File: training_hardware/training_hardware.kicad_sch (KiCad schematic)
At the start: 0 parts

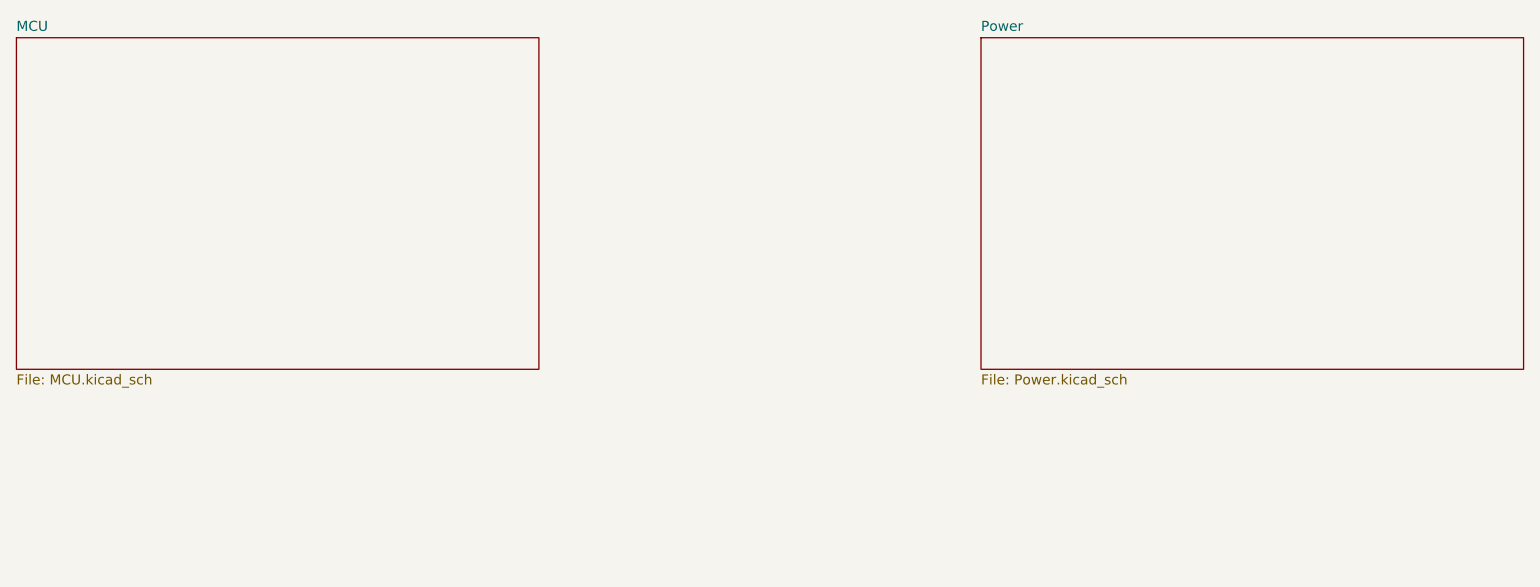
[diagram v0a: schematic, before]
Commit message: Add CAN Transceiver
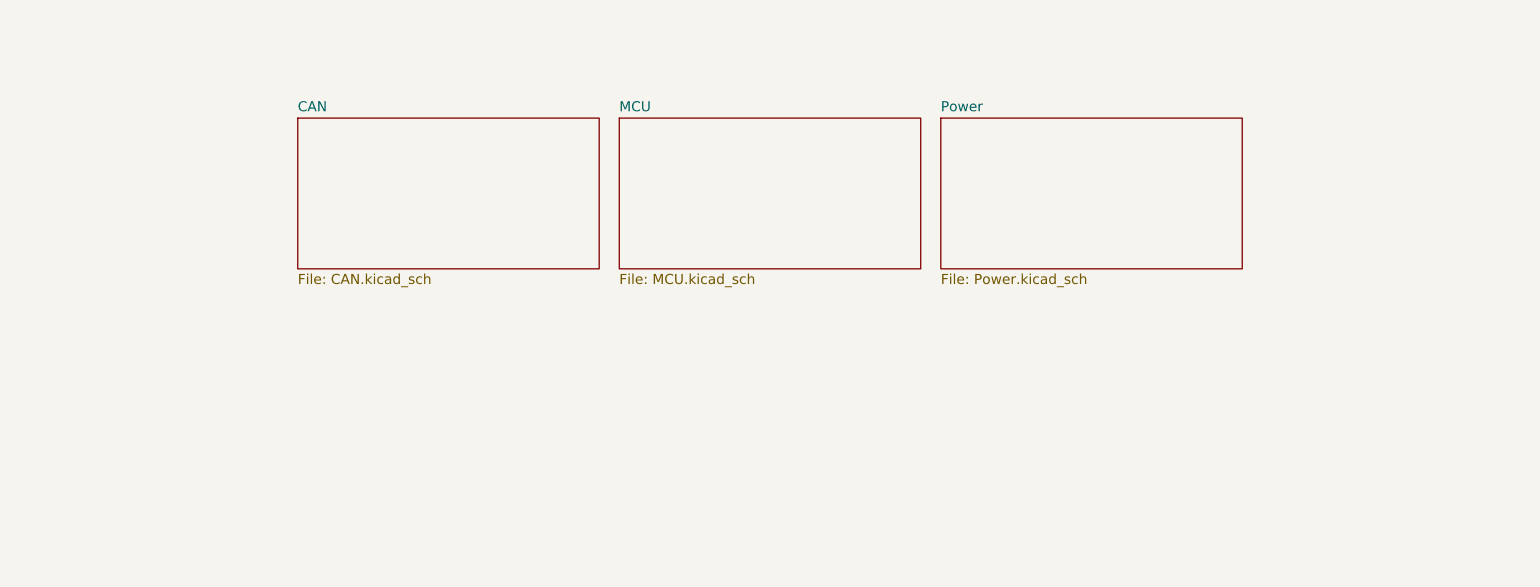
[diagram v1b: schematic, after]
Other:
- added sheet CAN (CAN.kicad_sch)
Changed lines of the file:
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@@
 	(paper "A4")
 	(sheet
-		(at 45.72 72.39)
-		(size 66.04 41.91)
+		(at 121.92 82.55)
+		(size 38.1 19.05)
 		(exclude_from_sim no)
 		(in_bom yes)
@@
 		)
 		(property "Sheetname" "MCU"
-			(at 45.72 71.6784 0)
+			(at 121.92 81.8384 0)
 			(effects
 				(font
@@
 		)
 		(property "Sheetfile" "MCU.kicad_sch"
-			(at 45.72 114.8846 0)
+			(at 121.92 102.1846 0)
 			(effects
 				(font
@@
 	)
 	(sheet
-		(at 167.64 72.39)
-		(size 68.58 41.91)
+		(at 162.56 82.55)
+		(size 38.1 19.05)
 		(exclude_from_sim no)
 		(in_bom yes)
@@
 		)
 		(property "Sheetname" "Power"
-			(at 167.64 71.6784 0)
+			(at 162.56 81.8384 0)
 			(effects
 				(font
@@
 		)
 		(property "Sheetfile" "Power.kicad_sch"
-			(at 167.64 114.8846 0)
+			(at 162.56 102.1846 0)
 			(effects
 				(font
@@
 				)
 			)
+		)
+	)
+	(sheet
+		(at 81.28 82.55)
+		(size 38.1 19.05)
+		(exclude_from_sim no)
+		(in_bom yes)
+		(on_board yes)
+		(dnp no)
+		(fields_autoplaced yes)
+		(stroke
+			(width 0.1524)
+			(type solid)
+		)
+		(fill
+			(color 0 0 0 0.0000)
+		)
+		(property "Sheetname" "CAN"
+			(at 81.28 81.8384 0)
+			(effects
+				(font
+					(size 1.27 1.27)
+				)
+				(justify left bottom)
+			)
+		)
+		(property "Sheetfile" "CAN.kicad_sch"
+			(at 81.28 102.1846 0)
+			(effects
+				(font
+					(size 1.27 1.27)
+				)
+				(justify left top)
+			)
+		)
+		(instances
+			(project "training_hardware"
+				(path "/4cf2d799-67ae-4e4e-ac38-46710a69e750"
+					(page "4")
+				)
+			)

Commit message: Finish Schematic
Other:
- sheet CAN ports: added RXD, STBY, TXD; removed none
- sheet MCU ports: added CRX1, CTX1, STBY; removed none
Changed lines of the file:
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@@
 	(generator_version "9.0")
 	(paper "A4")
+	(wire
+		(pts
+			(xy 119.38 88.9) (xy 125.73 88.9)
+		)
+		(stroke
+			(width 0)
+			(type default)
+		)
+	)
+	(wire
+		(pts
+			(xy 119.38 91.44) (xy 125.73 91.44)
+		)
+		(stroke
+			(width 0)
+			(type default)
+		)
+	)
+	(wire
+		(pts
+			(xy 119.38 86.36) (xy 125.73 86.36)
+		)
+		(stroke
+			(width 0)
+			(type default)
+		)
+	)
 	(sheet
-		(at 121.92 82.55)
+		(at 125.73 82.55)
 		(size 38.1 19.05)
 		(exclude_from_sim no)
@@
 		)
 		(property "Sheetname" "MCU"
-			(at 121.92 81.8384 0)
+			(at 125.73 81.8384 0)
 			(effects
 				(font
@@
 		)
 		(property "Sheetfile" "MCU.kicad_sch"
-			(at 121.92 102.1846 0)
+			(at 125.73 102.1846 0)
 			(effects
 				(font
@@
 				)
 				(justify left top)
+			)
+		)
+		(pin "CRX1" input
+			(at 125.73 86.36 180)
+			(effects
+				(font
+					(size 1.27 1.27)
+				)
+				(justify left)
+			)
+		)
+		(pin "CTX1" output
+			(at 125.73 91.44 180)
+			(effects
+				(font
+					(size 1.27 1.27)
+				)
+				(justify left)
+			)
+		)
+		(pin "STBY" output
+			(at 125.73 88.9 180)
+			(effects
+				(font
+					(size 1.27 1.27)
+				)
+				(justify left)
 			)
 		)
@@
 	)
 	(sheet
-		(at 162.56 82.55)
+		(at 170.18 82.55)
 		(size 38.1 19.05)
 		(exclude_from_sim no)
@@
 		)
 		(property "Sheetname" "Power"
-			(at 162.56 81.8384 0)
+			(at 170.18 81.8384 0)
 			(effects
 				(font
@@
 		)
 		(property "Sheetfile" "Power.kicad_sch"
-			(at 162.56 102.1846 0)
+			(at 170.18 102.1846 0)
 			(effects
 				(font
@@
 			)
 		)
+		(pin "RXD" output
+			(at 119.38 86.36 0)
+			(effects
+				(font
+					(size 1.27 1.27)
+				)
+				(justify right)
+			)
+		)
+		(pin "STBY" input
+			(at 119.38 88.9 0)
+			(effects
+				(font
+					(size 1.27 1.27)
+				)
+				(justify right)
+			)
+		)
+		(pin "TXD" input
+			(at 119.38 91.44 0)
+			(effects
+				(font
+					(size 1.27 1.27)
+				)
+				(justify right)
+			)
+		)

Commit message: Layout Training
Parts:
- added H1, H2: MountingHole, MRDT_Drill_Holes:4_40_Hole_Corner, symbol Mechanical:MountingHole
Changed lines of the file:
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@@
+		)
+	)
+	(symbol
+		(lib_id "Mechanical:MountingHole")
+		(at 83.82 130.81 0)
+		(unit 1)
+		(exclude_from_sim no)
+		(in_bom no)
+		(on_board yes)
+		(dnp no)
+		(fields_autoplaced yes)
+		(property "Reference" "H1"
+			(at 86.36 129.5399 0)
+			(effects
+				(font
+					(size 1.27 1.27)
+				)
+				(justify left)
+			)
+		)
+		(property "Value" "MountingHole"
+			(at 86.36 132.0799 0)
+			(effects
+				(font
+					(size 1.27 1.27)
+				)
+				(justify left)
+			)
+		)
+		(property "Footprint" "MRDT_Drill_Holes:4_40_Hole_Corner"
+			(at 83.82 130.81 0)
+			(effects
+				(font
+					(size 1.27 1.27)
+				)
+				(hide yes)
+			)
+		)
+		(property "Datasheet" "~"
+			(at 83.82 130.81 0)
+			(effects
+				(font
+					(size 1.27 1.27)
+				)
+				(hide yes)
+			)
+		)
+		(property "Description" "Mounting Hole without connection"
+			(at 83.82 130.81 0)
+			(effects
+				(font
+					(size 1.27 1.27)
+				)
+				(hide yes)
+			)
+		)
+		(instances
+			(project ""
+				(path "/4cf2d799-67ae-4e4e-ac38-46710a69e750"
+					(reference "H1")
+					(unit 1)
+				)
+			)
+		)
+	)
+	(symbol
+		(lib_id "Mechanical:MountingHole")
+		(at 83.82 137.16 0)
+		(unit 1)
+		(exclude_from_sim no)
+		(in_bom no)
+		(on_board yes)
+		(dnp no)
+		(fields_autoplaced yes)
+		(property "Reference" "H2"
+			(at 86.36 135.8899 0)
+			(effects
+				(font
+					(size 1.27 1.27)
+				)
+				(justify left)
+			)
+		)
+		(property "Value" "MountingHole"
+			(at 86.36 138.4299 0)
+			(effects
+				(font
+					(size 1.27 1.27)
+				)
+				(justify left)
+			)
+		)
+		(property "Footprint" "MRDT_Drill_Holes:4_40_Hole_Corner"
+			(at 83.82 137.16 0)
+			(effects
+				(font
+					(size 1.27 1.27)
+				)
+				(hide yes)
+			)
+		)
+		(property "Datasheet" "~"
+			(at 83.82 137.16 0)
+			(effects
+				(font
+					(size 1.27 1.27)
+				)
+				(hide yes)
+			)
+		)
+		(property "Description" "Mounting Hole without connection"
+			(at 83.82 137.16 0)
+			(effects
+				(font
+					(size 1.27 1.27)
+				)
+				(hide yes)
+			)
+		)
+		(instances
+			(project "training_hardware"
+				(path "/4cf2d799-67ae-4e4e-ac38-46710a69e750"
+					(reference "H2")
+					(unit 1)
+				)
+			)
 		)
 	)
